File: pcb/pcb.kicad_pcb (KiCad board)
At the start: 2 copper layers, 63.8 x 43.2 mm, 38 parts, among them J1 BAT+, J10 GRN, J11 RED, J12 Load Cell, J2 BAT-, J3 Molex, J4 TMP37, J5 TMP+, J6 TMPO, J7 TMP-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

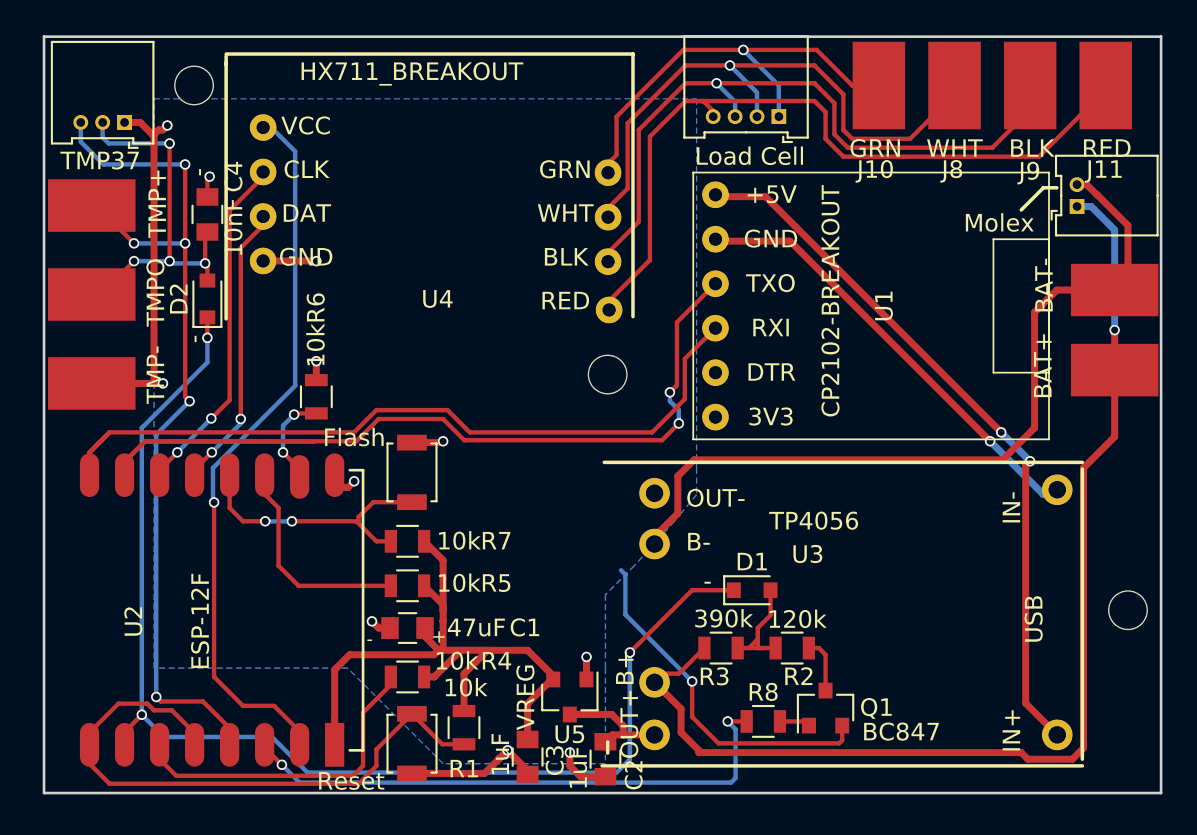
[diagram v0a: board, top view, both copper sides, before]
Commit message: Switch to p-channel MOSFET for battery monitor switch
Because we want as close to zero voltage through the circuit to the
ADC as possible when the battery monitor is off and the temperature
sensor is on, we need to switch on the high side, between BAT+ and
ADC.

The BSS84 seems like a reasonable choice; its maximum gate threshold
voltage is well below the difference between ground and a discharged
li-ion at 2.7V. I don't really care about pulling it up to 3.3 so
that it keeps the battery circuit off; it's the difference between
a hundred nanoamps and six or eight microamps.
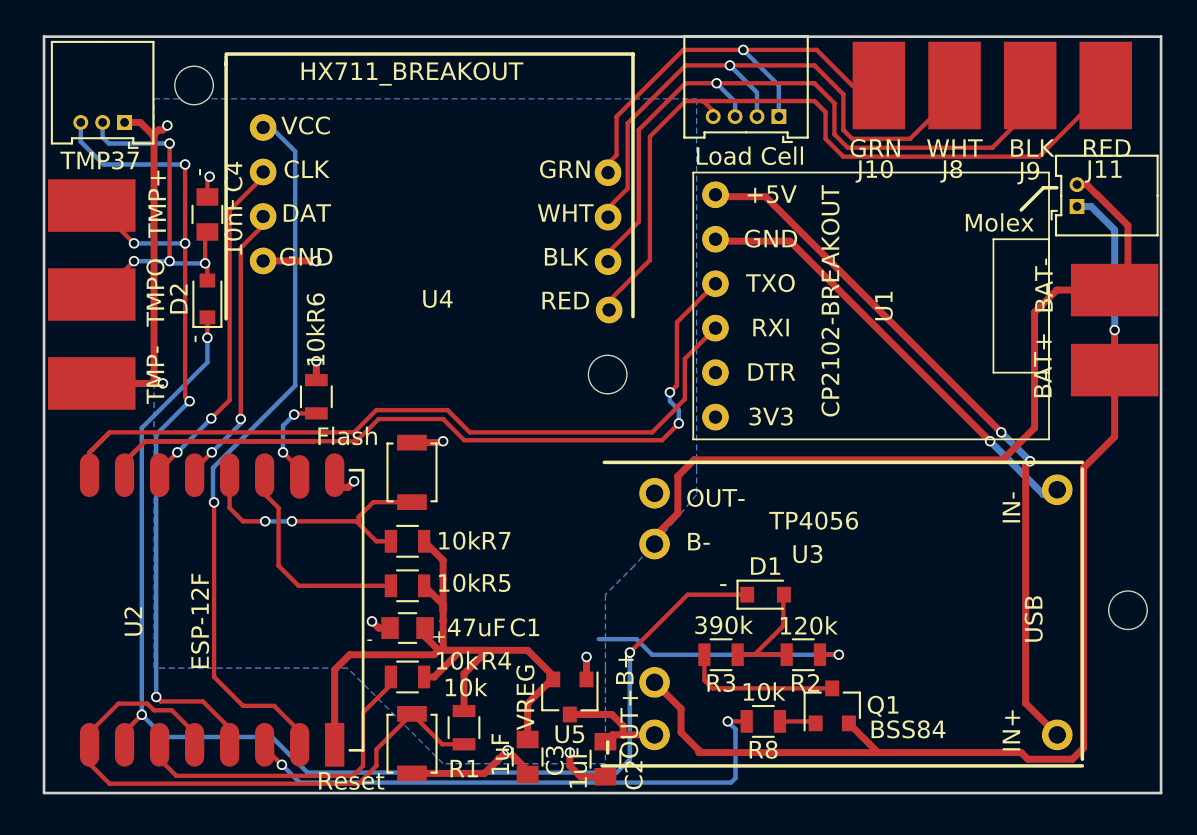
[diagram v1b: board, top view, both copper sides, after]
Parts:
- Q1: value BC847 -> BSS84
- moved D1 0.80 mm to (147.4, 97.4)
- moved R2 0.74 mm to (149.6, 100.8)
- moved Q1 0.40 mm to (151.3, 103.8)
- moved R3 0.38 mm to (144.9, 100.8)
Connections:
- Q1 pad 2: /GND -> /BAT+
- R2 pad 2: Net-(Q1-Pad3) -> /GND
- R3 pad 2: /BAT+ -> Net-(Q1-Pad3)
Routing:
- net Net-(Q1-Pad3): track 3.16 -> 8.95 mm
- net /GND: track 63.8 -> 58.8 mm
- net /BAT+: track 64.9 -> 63.9 mm
- net /ADC: track 70.0 -> 70.6 mm

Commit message: DS18B20, 4x3 switch footprint, routing tweaks
Use a DS18B20 temperature sensor instead of a TMP36. We have enough
GPIOs—we can drive it from the former SENS2 net (power for the prior
sensor) and use the former SENS1 net (battery monitor transistor) for
the data line. This simplifies the ADC circuitry significantly, and
lets us ditch a bunch of parts.

Add 4mmx3mm switch footprint, adjust routing as needed.
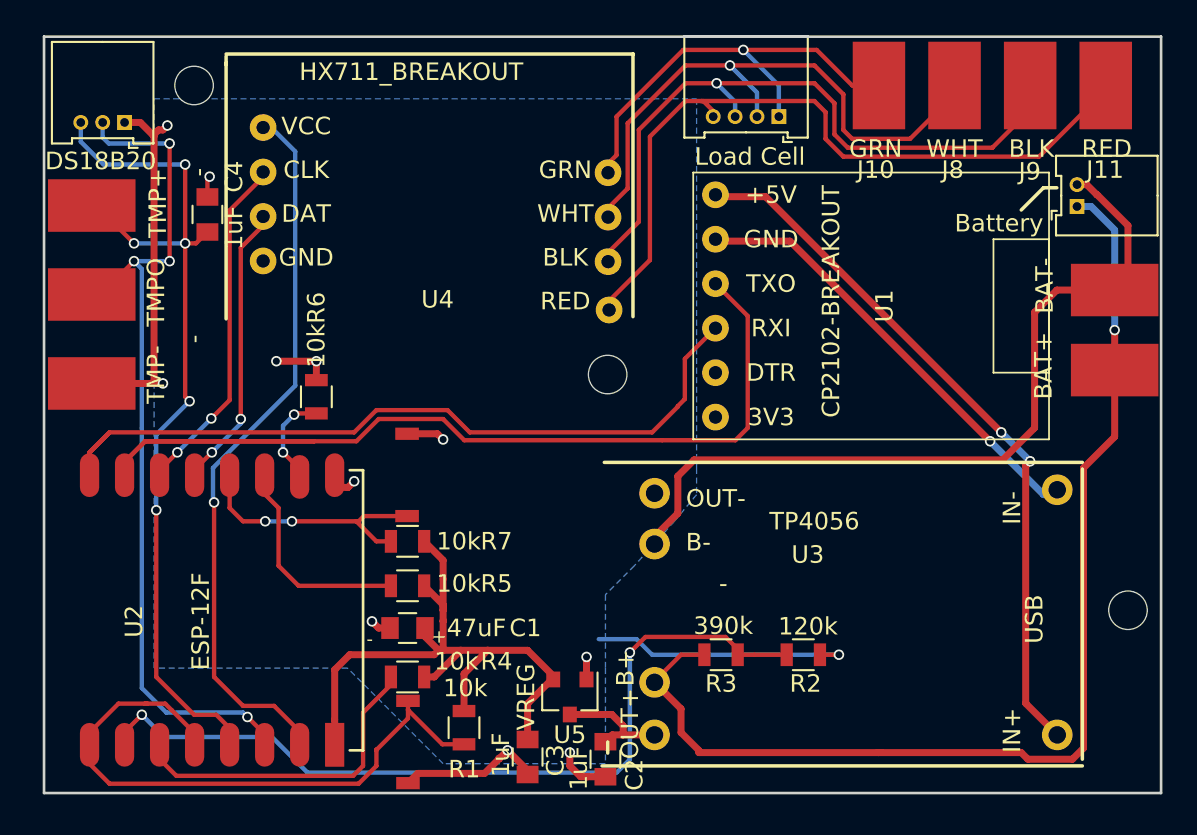
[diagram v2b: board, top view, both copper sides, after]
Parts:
- removed D1, D2: D, Diodes_SMD:D_0805
- removed Q1: BSS84, TO_SOT_Packages_SMD:SOT-23
- removed R8: 10k, Resistors_SMD:R_0805
- C4: value 10nF -> 1uF
- J3: value Molex -> Battery
- J4: value TMP37 -> DS18B20
- SW1, SW2: footprint Buttons_Switches_SMD:SW_SPST_B3U-1000P -> 4x3_SWITCH:4x3_Switch
- moved SW1 3.34 mm to (125.4, 103.1), turned to 0 degrees
- moved SW2 3.14 mm to (128.6, 93.3), turned to 180 degrees
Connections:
- C4 pad 2: /TMPO -> /DS+
- J4 pad 2: /TMPO -> /DSD
- J4 pad 3: /SENS2 -> /DS+
- J5 pad 1: /SENS2 -> /DS+
- J6 pad 1: /TMPO -> /DSD
- R2 pad 1: Net-(D1-Pad2) -> /ADC
- R3 pad 1: Net-(D1-Pad2) -> /ADC
- R3 pad 2: Net-(Q1-Pad3) -> /BAT+
- U2 pad 5: /SENS2 -> /DS+
- U2 pad 6: /SENS1 -> /DSD
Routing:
- net /DS+: track 0.00 -> 51.4 mm, vias 0 -> 5
- net /DSD: track 0.00 -> 50.4 mm, vias 0 -> 4
- net /SENS2: track 50.3 -> 0.00 mm, vias 5 -> 0
- net /SENS1: track 33.3 -> 0.00 mm, vias 2 -> 0
- net /ADC: track 70.6 -> 48.3 mm, vias 3 -> 2
- net /TMPO: track 21.7 -> 0.00 mm, vias 4 -> 0
- net Net-(Q1-Pad3): track 8.95 -> 0.00 mm
- net Net-(D1-Pad2): track 6.93 -> 0.00 mm
- net /HostTX: track 55.6 -> 59.2 mm, vias 2 -> 0
- net Net-(Q1-Pad1): track 2.08 -> 0.00 mm
- net /BAT+: track 63.9 -> 65.1 mm
- net Net-(R1-Pad2): track 33.9 -> 35.1 mm
- net Net-(R7-Pad2): track 14.9 -> 14.2 mm

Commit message: Add capacitors across TP4056 OUT+/OUT-
I'm told this will fake a battery sufficiently well to keep from
confusing the TP4056 in the no-battery case. The two 47uF capacitors
can run the whole PCB in sleep mode for 2-3 seconds, and presumably
the non-sleep-mode load is sufficient to fool the TP4056.

I guess we'll see!
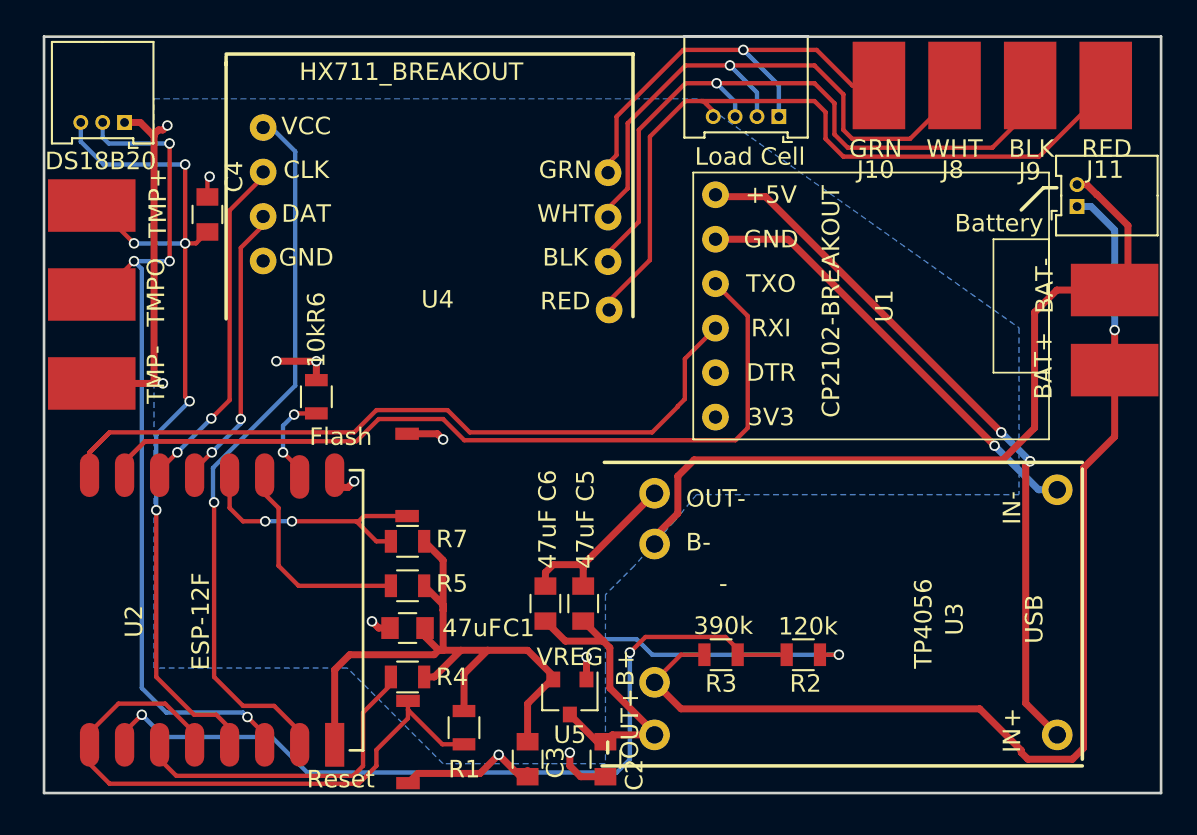
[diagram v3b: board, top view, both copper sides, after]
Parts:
- removed ? (x3): , Mounting_Holes:MountingHole_2.2mm_M2
- removed G***: LOGO, OSHW:LOGO_5mm
- added C5: 47uF, Capacitors_SMD:C_0805, F.Cu at (137.0, 97.9)
- added C6: 47uF, Capacitors_SMD:C_0805, F.Cu at (134.9, 97.9)
- moved C3 0.13 mm to (133.9, 106.8)
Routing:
- net /CHG+: track 6.80 -> 17.6 mm
- net /GND: track 58.9 -> 68.8 mm
- net /BAT+: track 65.1 -> 64.1 mm
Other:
- board text removed: "+"

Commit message: Another crack at a battery disconnector circuit
I found an example on the Arduino forums (link at end). It uses a
p-channel MOSFET 'backwards', with source connected to the load
and drain to the battery. The parasitic diode therefore blocks
leakage back into the battery. USB is connected to the gate and also
to the load, the latter via Schottky diode, to prevent battery
voltage from sneaking back through the circuit to flip the MOSFET.

A large capacitor buffers between the voltage regulator and ground,
to ensure that the system doesn't lose power while things are switching.
(The MOSFET takes on the order of nanoseconds to switch; the 47uF
capacitor between VREG+ and GND can run the ESP at peak current for
about 15 milliseconds, and the ESP has its own 47uF capacitor, too.)

You can see the circuit in action here: https://www.systemvision.com/design/pendulum-pcb-battery-disconnector/

Forum thread here: http://forum.arduino.cc/index.php?topic=496727.0
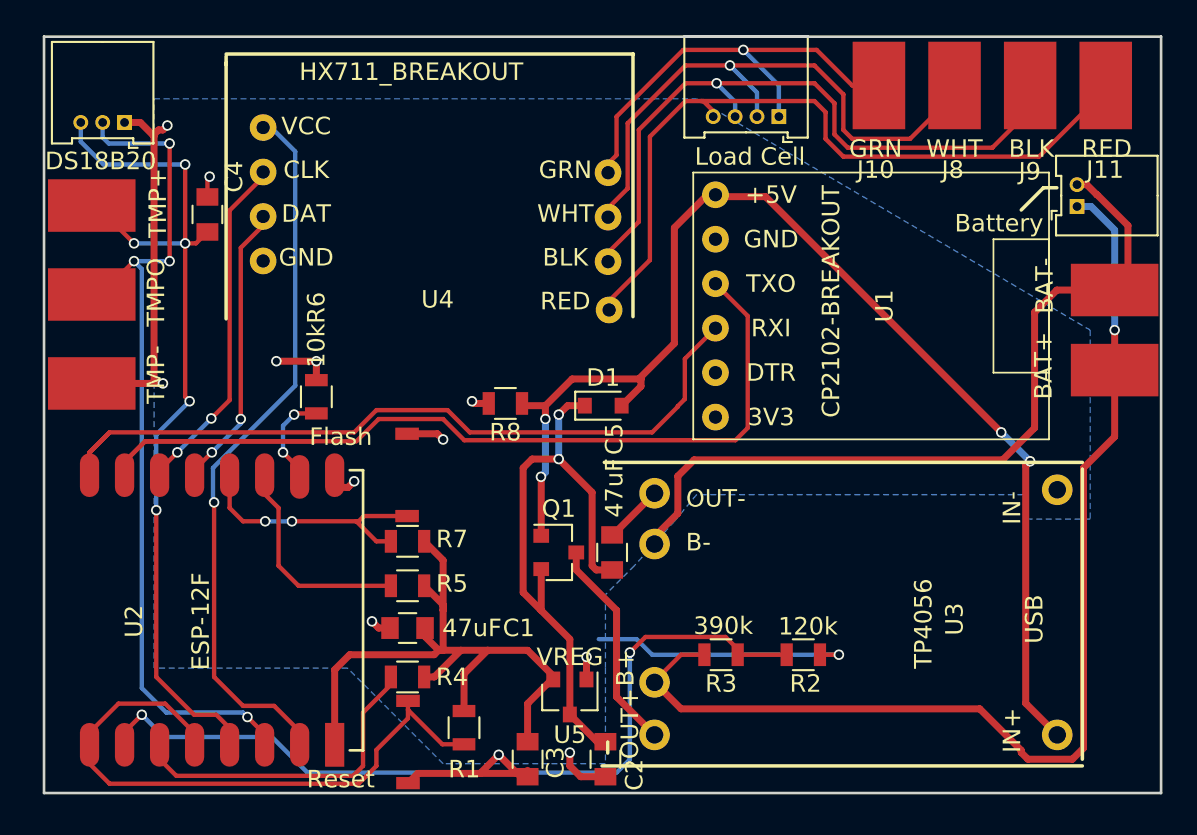
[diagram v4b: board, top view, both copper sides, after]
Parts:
- removed C6: 47uF, Capacitors_SMD:C_0805
- added D1: D_Schottky, Diodes_SMD:D_0805, F.Cu at (138.2, 86.6)
- added Q1: AO3401, TO_SOT_Packages_SMD:SOT-23, F.Cu at (135.6, 95.0)
- added R8: 10k, Resistors_SMD:R_0805, F.Cu at (132.6, 86.5)
- moved C5 3.36 mm to (138.7, 95.0)
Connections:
- C2 pad 2: /CHG+ -> /VREG+
- C5 pad 1: /CHG+ -> /VREG+
- U1 pad 5: /USB- -> /GND
- U3 pad 2: /USB- -> /GND
- U5 pad 3: /CHG+ -> /VREG+
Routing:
- net /VREG+: track 0.00 -> 34.8 mm, vias 0 -> 2
- net /USB+: track 40.8 -> 70.5 mm, vias 2 -> 4
- net /USB-: track 25.4 -> 0.00 mm, vias 1 -> 0
- net /CHG+: track 17.6 -> 12.4 mm
- net /GND: track 68.8 -> 65.9 mm, vias 12 -> 13
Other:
- board text removed: "-"

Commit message: pcb-1.0.0-rc.3
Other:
- board text added: "1.0.0-rc.3"
- board text removed: "1.0.0-rc.2"
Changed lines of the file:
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@@
     (links 66)
     (no_connects 0)
-    (area 106.162999 65.462999 170.113001 108.813001)
+    (area 99.863999 58.638 182.188 114.438001)
     (thickness 1.6)
     (drawings 21)
@@
     (title "Pendulum PCB")
     (date 2018-06-24)
-    (rev 1.0.0-rc.2)
+    (rev 1.0.0-rc.3)
   )
   (layers
@@
   )
   (setup
-    (last_trace_width 0.4)
+    (last_trace_width 0.25)
     (user_trace_width 0.4)
     (trace_clearance 0.2)
@@
     (arrow2b (pts (xy 100.138 111.738) (xy 101.264504 111.151579)))
   )
-  (gr_text 1.0.0-rc.2 (at 113.638 98.138 270) (layer B.SilkS)
+  (gr_text 1.0.0-rc.3 (at 113.638 98.138 270) (layer B.SilkS)
     (effects (font (size 1 1) (thickness 0.15)) (justify mirror))
   )
